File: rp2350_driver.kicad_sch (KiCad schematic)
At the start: 256 parts, among them J1 Power Input, J2 CAN2 PLUG, J201 Estop Conn, J202 USB_C_Receptacle_USB2.0, J203 Conn_01x06, J204 SM03B-SRSS-TB, J205 Power Output, J206 SM03B-SRSS-TB, J207 Conn_01x03, J208 Conn_01x03, J21 Power Input, J3 Power Input, Q1 Q_PNP_BEC, Q2 Q_PNP_BEC, Q201 Q_PNP_BEC, Q3 Q_PNP_BEC, SW201 Boot, SW202 Reset, U1 INA240A1D, U10 SIT3088ETK, U11 TS5A3159DCK, U12 SIT3088ETK, U13 TS5A3159DCK, U14 TS5A3159DCK, U15 TS5A3159DCK, U16 TS5A3159DCK, U17 TS5A3159DCK, U2 EG3113, U201 EG3113, U202 SPX3819M5-L-3-3, U203 RP2350_80QFN, U204 W25Q16JV, U21 INA240A1D, U3 USBLC6-2P6, U4 TX4137, U44 INA240A1D, U5 EG3113, U6 CA-IS3052G, U7 SIT3088ETK, U8 EG3113, U9 SIT3088ETK, Y201 ABM8-272-T3

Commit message: All components in board footprint. Big readme update.
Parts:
- added C30, C33, C34, C35, C36: 100n, Capacitor_SMD:C_0402_1005Metric, symbol Device:C
- added R21, R34, R37, R38, R39, R42, R43, R44: 10k, Resistor_SMD:R_0402_1005Metric, symbol Device:R
- added U18, U19, U20, U22: TS5A3159DCK, Package_TO_SOT_SMD:SOT-353_SC-70-5, symbol integrated:TS5A3159
- SW201, SW202: footprint Button_Switch_SMD:SW_Push_1P1T_NO_Vertical_Wuerth_434133025816 -> parts:KEY-SMD_4P-L4.2-W3.2-P2.20-LS4.6; LCSC (none) -> C19724063
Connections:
- net GPIO14 is gone; now on net V_SW: U203.13 (GPIO14)
- net GPIO15 is gone; now on net I2C_SW: U203.14 (GPIO15)
- net GPIO32 is gone; now on net HALL2: U203.40 (GPIO32)
- net GPIO33 is gone; now on net HALL3: U203.42 (GPIO33)
- net GPIO34 is gone; now on net H1_SW: U203.43 (GPIO34)
- net GPIO35 is gone; now on net H2_SW: U203.44 (GPIO35)
- net GPIO36 is gone; now on net H3_SW: U203.45 (GPIO36)
- net +3V3: now also C36.1, R21.2, R37.2, R39.2, R43.2
- net B_PHASE_SENSE: now also U22.3 (NC); no longer U203.55 (GPIO44_ADC4)
- net C_PHASE_SENSE: now also U20.3 (NC); no longer U203.56 (GPIO45_ADC5)
- net ENC_A_N: now also U14.4 (COM); no longer FL1.2
- net ENC_A_P: no longer FL1.3
- net ENC_B_N: now also U17.4 (COM); no longer FL2.2
- net ENC_B_P: now also U16.4 (COM); no longer FL2.3, U14.4 (COM)
- net ENC_C_N: now also U19.4 (COM); no longer FL3.2
- net ENC_C_P: now also U18.4 (COM); no longer FL3.3, U16.4 (COM)
- net ENC_D_N: now also R43.1, R44.2
- net ENC_D_P: now also FL4.3; no longer U17.4 (COM)
- net GND: now also C30.2, C33.2, C34.2, C35.2, C36.2, R34.1, R38.1, R42.1, R44.1, U18.2 (GND), U19.2 (GND), U20.2 (GND), U22.2 (GND)
- net HALL1: now also U203.39 (GPIO31)
- net Vdrive: now also C30.1, C33.1, C34.1, C35.1, U18.5 (V+), U19.5 (V+), U20.5 (V+), U22.5 (V+)
- net ENC_A_N_SW: now reaches U14.3 (NC)
- net ENC_A_N_SW: now also FL1.2, R39.1, R42.2
- net ENC_A_P_SW: now reaches U13.3 (NC)
- net ENC_A_P_SW: now also FL1.3
- net ENC_B_P_SW: now reaches U16.3 (NC)
- net ENC_B_P_SW: now also FL2.3
- net ENC_D_P_SWITCHED renamed ENC_B_N_SW
- net ENC_B_N_SW: now also FL2.2, R37.1, R38.2; no longer FL4.3
- net GPIO37 renamed EXT_ANALOG_SW
- net EXT_ANALOG_SW: now also U18.6 (ENB), U19.6 (ENB), U20.6 (ENB), U22.6 (ENB)
- net GPIO38: no longer names the net of U203.47 (GPIO38)
- net GPIO39: no longer names the net of U203.48 (GPIO39)
- new net ADC4: U203.55 (GPIO44_ADC4), U22.1 (NO)
- new net ADC5: U20.1 (NO), U203.56 (GPIO45_ADC5)
- new net ENC_C_N_SW: FL3.2, R21.1, R34.2, U19.3 (NC)
- new net ENC_C_P_SW: FL3.3, U18.3 (NC)
- new net EXT_ANALOG1: U18.1 (NO), U22.4 (COM)
- new net EXT_ANALOG2: U19.1 (NO), U20.4 (COM)
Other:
- note added: "Divider for single ended use without hall filtering."
- note added: "Encoder Supports: Single Ended I2C Hall Sensors Differential or Single Ended SPI Differential or Single Ended Quadrature with Index Dual Channel Analog"
- note added: "GIRL ARE YOUR ENCODERS NUMERICALLY OR ALPHABETICALLY INDEXED MAKE A GODDAMN DECISION"
- note added: "When using halls, route signals through this filter network."
- note removed: "IF ANALOG SWITCHES LET US ROUTE SINGLE ENDED TO OTHER GPIO PINS THEN WE DON'T NEED DEDICATED I2C PINS"
- note removed: "Preferred connections: Differential I2C (Will choose single ended for now) Hall Sensors (single ended) Differential SPI Differential Quadrature with Index No planned support for analog (could add SPI converter)"
- moved on the sheet: C14, C16, C19, C20, C22, C26, C27, C28, C31, C32, R19, R20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

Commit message: 100 percent routed and no DRC errors! needs massive review still.
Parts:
- C47: renamed from C219; LCSC (none) -> C15850
- U13: renamed from U20; footprint Package_TO_SOT_SMD:SOT-353_SC-70-5 -> Package_TO_SOT_SMD:SOT-363_SC-70-6
- U14: renamed from U22; footprint Package_TO_SOT_SMD:SOT-353_SC-70-5 -> Package_TO_SOT_SMD:SOT-363_SC-70-6
- U15: footprint Package_TO_SOT_SMD:SOT-353_SC-70-5 -> Package_TO_SOT_SMD:SOT-363_SC-70-6
- U17: renamed from U11; footprint Package_TO_SOT_SMD:SOT-353_SC-70-5 -> Package_TO_SOT_SMD:SOT-363_SC-70-6
- U22: renamed from U13; footprint Package_TO_SOT_SMD:SOT-353_SC-70-5 -> Package_TO_SOT_SMD:SOT-363_SC-70-6
- U23: renamed from U16; footprint Package_TO_SOT_SMD:SOT-353_SC-70-5 -> Package_TO_SOT_SMD:SOT-363_SC-70-6
- U24: renamed from U18; footprint Package_TO_SOT_SMD:SOT-353_SC-70-5 -> Package_TO_SOT_SMD:SOT-363_SC-70-6
- U25: renamed from U19; footprint Package_TO_SOT_SMD:SOT-353_SC-70-5 -> Package_TO_SOT_SMD:SOT-363_SC-70-6
- U26: renamed from U14; footprint Package_TO_SOT_SMD:SOT-353_SC-70-5 -> Package_TO_SOT_SMD:SOT-363_SC-70-6
- U27: renamed from U17; footprint Package_TO_SOT_SMD:SOT-353_SC-70-5 -> Package_TO_SOT_SMD:SOT-363_SC-70-6
- renumbered AH2 to AH1, AL2 to AL1, BH2 to BH1, BL2 to BL1, C77 to C1, C70 to C10, C10 to C11, C202 to C12, C221 to C13, C222 to C14, C11 to C15, C66 to C16, C216 to C17, C217 to C18, C4 to C19, C15 to C2, C203 to C20, C215 to C21, C204 to C22, C25 to C23, C205 to C24, C106 to C25, C105 to C26, C2 to C27, C13 to C28, C1 to C29, C12 to C3, C206 to C30, C9 to C31, C207 to C32, C103 to C33, C104 to C34, C208 to C35, C65 to C36, C209 to C37, C210 to C38, C6 to C39, C218 to C4, C74 to C40, C211 to C41, C3 to C42, C212 to C43, C78 to C44, C213 to C45, C214 to C46, C220 to C48, C34 to C49, C201 to C5, C35 to C50, C233 to C51, C29 to C52, C234 to C53, C235 to C54, C236 to C55, C36 to C56, C5 to C57, C7 to C58, C23 to C59, C17 to C6, C21 to C60, C8 to C61, C18 to C62, C24 to C63, C26 to C64, C28 to C65, C30 to C66, C19 to C67, C31 to C68, C20 to C69, C101 to C7, C32 to C70, C33 to C71, C14 to C72, C22 to C73, C16 to C74, C27 to C75, C79 to C8, C102 to C9, CH2 to CH1, CH201 to CH2, CL2 to CL1, CL201 to CL2, D202 to D1, D2 to D10, D16 to D11, D15 to D12, D8 to D13, D10 to D14, D6 to D15, D5 to D16, D9 to D17, D203 to D18, D204 to D19, D207 to D2, D205 to D20, D206 to D21, D4 to D22, D19 to D23, D20 to D24, D21 to D25, D22 to D26, D23 to D27, D7 to D3, D201 to D4, D1 to D5, D17 to D6, D14 to D7, D3 to D8, D18 to D9, FL2 to FL1, FL1 to FL2, J3 to J1, J205 to J10, J2 to J11, J203 to J12, J1 to J2, J202 to J3, J206 to J4, J201 to J5, J204 to J6, J207 to J7, J208 to J8, J21 to J9, L201 to L2, Q3 to Q1, Q1 to Q2, Q2 to Q3, Q201 to Q4, R120 to R1, R31 to R10, R30 to R11, R112 to R12, R33 to R13, R32 to R14, R36 to R15, R11 to R16, R86 to R17, R87 to R18, R12 to R19, R119 to R2, R105 to R20, R121 to R21, R122 to R22, R113 to R23, R208 to R24, R26 to R25, R211 to R26, R18 to R27, R2 to R28, R22 to R29, R238 to R3, R25 to R30, R24 to R31, R201 to R32, R23 to R33, R206 to R34, R123 to R35, R124 to R36, R91 to R37, R90 to R38, R4 to R39, R239 to R4, R5 to R40, R1 to R41, R8 to R42, R9 to R43, R7 to R44, R27 to R45, R28 to R46, R29 to R47, R88 to R48, R45 to R49, R240 to R5, R202 to R50, R203 to R51, R89 to R52, R225 to R53, R224 to R54, R109 to R55, R114 to R56, R16 to R57, R17 to R58, R6 to R59, R212 to R6, R10 to R60, R13 to R61, R204 to R62, R205 to R63, R207 to R64, R227 to R65, R228 to R66, R209 to R67, R210 to R68, R220 to R69, R213 to R7, R221 to R70, R222 to R71, R223 to R72, R229 to R73, R230 to R74, R231 to R75, R232 to R76, R233 to R77, R234 to R78, R235 to R79, R226 to R8, R236 to R80, R237 to R81, R14 to R82, R15 to R83, R35 to R84, R40 to R85, R37 to R86, R38 to R87, R39 to R88, R42 to R89, R3 to R9, R43 to R90, R44 to R91, R21 to R92, R34 to R93, R20 to R94, R41 to R95, R19 to R96, SW201 to SW1, SW202 to SW2, TP81 to TP1, TP208 to TP10, TP73 to TP2, TP74 to TP3, TP77 to TP4, TP64 to TP5, TP66 to TP6, TP94 to TP7, TP71 to TP8, TP207 to TP9, U8 to U1, U44 to U10, U3 to U11, U201 to U12, U6 to U16, U12 to U18, U7 to U19, U4 to U2, U9 to U20, U10 to U21, U204 to U3, U202 to U4, U21 to U5, U5 to U6, U2 to U7, U203 to U8, U1 to U9, Y201 to Y1
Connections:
- net +5V is gone; now on net Vdrive: C15.2, C2.2, C27.2, C48.2, D10.2 (A), D14.2 (A), D18.2 (A), D3.2 (A), U1.1 (VCC), U12.1 (VCC), U6.1 (VCC), U7.1 (VCC)
- no-connect marks 2 -> 1
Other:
- moved on the sheet: C11, C12, C3, C4, C5, D1, D2, D4, D8, J3, J4, J5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

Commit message: Cleaned up schematic encoder layout, fixed a sch/layout bug.
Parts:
- added D28, D29: 5V TVS, Package_TO_SOT_SMD:SOT-883, symbol Power_Protection:SP0502BAHT
- added TP12, TP13, TP14, TP15, TP16, TP17, TP18, TP19: TestPoint, TestPoint:TestPoint_Pad_D1.0mm, symbol Connector:TestPoint
- C11, C47: value 10u -> 10u 25v
- C12, C5: value 10u -> 10u 25v; LCSC (none) -> C15850
- C15, C2, C27, C48, C58: LCSC C162274 -> C329940
- C20, C24, C30, C32, C35, C37, C38, C41, C43, C45, C46: LCSC C14663 -> C131394
- C67, C68, C74: LCSC C60137 -> C20069324
- D13, D17, D21, D9: LCSC C726760 -> C366557
- J1, J2: value Power Input -> XT30; LCSC C2918078 -> C431092; Note (none) -> Phase Output
- J10: LCSC C7363338 -> C2913282
- J4, J6: LCSC C160403 -> C2763613
- J7: LCSC (none) -> C492411
- J8: LCSC (none) -> C2897385
- J9: value Power Input -> XT30; LCSC C2918078 -> C431092; Name (none) -> Power Input
- L2: LCSC (none) -> C42411119
- R3, R4, R59, R60, R62, R63, R67, R68, R70, R71: LCSC C304067 -> C861451
- R32: value 33 -> 33R; LCSC (none) -> C25105
- R53, R54: value 100 -> 100R
- SW1: value Boot -> Button; Name (none) -> Boot
- SW2: value Reset -> Button; Name (none) -> Reset
- U16: value CA-IS3052G -> CA-IS3052CG; LCSC C528764 -> C41784142
- U8: LCSC (none) -> C42415655
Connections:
- net ADC4: now also U14.4 (COM); no longer U14.1 (NO)
- net ADC5: now also U13.4 (COM); no longer U13.1 (NO)
- net A_PWM_H: now also TP14.1
- net A_PWM_L\: now also TP15.1
- net B_PWM_H: now also TP17.1
- net B_PWM_L\: now also TP16.1
- net C_PWM_H: now also TP12.1
- net C_PWM_L\: now also TP13.1
- net D_PWM_H: now also TP19.1
- net D_PWM_L\: now also TP18.1
- net EXT_ANALOG1: now also U14.1 (NO); no longer U14.4 (COM)
- net EXT_ANALOG2: now also U13.1 (NO); no longer U13.4 (COM)
- net GND: now also D28.3 (A), D29.3 (A)
- net RXI_INTERBOARD_1: now also D28.2 (K)
- net RXI_INTERBOARD_2: now also D29.2 (K)
- net TXO_INTERBOARD_1: now also D28.1 (K)
- net TXO_INTERBOARD_2: now also D29.1 (K)
- net ENC1_D renamed ENC_A_DATA
- net ENC1_E renamed ENC_A_SW
- net ENC2_D renamed ENC_B_DATA
- net ENC2_E renamed ENC_B_SW
- net ENC3_D renamed ENC_C_DATA
- net ENC3_E renamed ENC_C_SW
- net ENC4_D renamed ENC_D_DATA
- net ENC4_E renamed ENC_D_SW
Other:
- note added: "CPU: Analog Halls I2C"
- note added: "CPU: Single Ended I/O"
- note added: "Differential tranceivers"
- note added: "EXT_ANALOG_SW can be shared. We either read external lines or those go to differential transceivers and we read B and C phase sense with analog."
- note added: "Encoder I/O"
- note added: "I/O Switching"
- note added: "Motor Phase B/C Sense"
- note removed: "GIRL ARE YOUR ENCODERS NUMERICALLY OR ALPHABETICALLY INDEXED MAKE A GODDAMN DECISION"
- moved on the sheet: C47, C49, C50, C59, C60, C61, C62, C63, C64, C65, C66, C67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

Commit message: Added USB-C PD, updated silk.
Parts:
- removed D4: B5819W SL, Diode_SMD:D_SOD-123, symbol Diode:MBR340
- removed R5: 5.1k 0.1%, Resistor_SMD:R_0603_1608Metric, symbol MotorController:TAYLOR_RESISTOR
- added C105, C106, C78: 4.7uF 50V X5R, Capacitor_SMD:C_0805_2012Metric, symbol Device:C
- added C107, C108: 330pF 50V, Capacitor_SMD:C_0402_1005Metric, symbol Device:C
- added C76: 100n, Capacitor_SMD:C_0402_1005Metric, symbol Device:C
- added C77: 4.7u, Capacitor_SMD:C_0402_1005Metric, symbol Device:C
- added R5: 470k, Resistor_SMD:R_0402_1005Metric, symbol Device:R
- added TP20: TestPoint, TestPoint:TestPoint_Pad_D1.0mm, symbol Connector:TestPoint
- added U101: FUSB302BMPX, Package_DFN_QFN:WQFN-14-1EP_2.5x2.5mm_P0.5mm_EP1.45x1.45mm, symbol Interface_USB:FUSB302BMPX
- added U28: LM73100RPWR, LM73100RPWR:IC_LM73100RPWR, symbol LM73100RPWR:LM73100RPWR
- R6: value 5.1k -> 165k; footprint Resistor_SMD:R_0603_1608Metric -> Resistor_SMD:R_0402_1005Metric; LCSC C23186 -> (none)
- R7: value 5.1k -> 39.2k; footprint Resistor_SMD:R_0603_1608Metric -> Resistor_SMD:R_0402_1005Metric; LCSC C23186 -> (none)
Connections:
- net +3V3: now also C76.1, C77.1, U101.12 (VCONN), U101.13 (VCONN), U101.3 (VDD), U101.4 (VDD)
- net A_N: now also D17.1 (A1), J1.1 (Pin_1), R55.2, R56.2, U10.8 (+); no longer D9.1 (A1), J2.1 (Pin_1), R20.2, R23.2, U5.8 (+)
- net C_N: now also D9.1 (A1), J2.1 (Pin_1), R20.2, R23.2, U5.8 (+); no longer D17.1 (A1), J1.1 (Pin_1), R55.2, R56.2, U10.8 (+)
- net GND: now also R7.1, C105.2, C106.2, C107.1, C108.1, C76.2, C77.2, C78.2, U101.15 (GND), U101.8 (GND), U101.9 (GND), U28.8 (GND), U28.9 (IMON); no longer R6.1, R7.2
- net I2C_SCL: now also U101.6 (SCL)
- net I2C_SDA: now also U101.7 (SDA)
- net VBUS: now also C105.1, C106.1, R5.2, U101.2 (VBUS), U28.5 (IN)
- net VMOT: now also C78.1, U28.6 (OUT)
- net at J3.B5 (CC2): now also C107.2, U101.1 (CC2), U101.14 (CC2); no longer R7.1
- net at U8.47 (GPIO38): now also TP20.1
- net PD_INT: now reaches U8.48 (GPIO39)
- net PD_INT: now also U101.5 (INT_N)
- net at R6.2: now also R5.1, U28.1 (EN/UVLO); no longer J3.A5 (CC1)
- new net: R6.1, R7.2, U28.2 (OVLO)
- new net: C108.2, J3.A5 (CC1), U101.10 (CC1), U101.11 (CC1)
- no-connect marks 1 -> 4
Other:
- note added: "Additional Switching"
- note added: "EXT_ANALOG_SW can be shared. We either route external lines to the ADC or those lines go to differential transceivers and we read B and C phase sense with analog."
- note added: "R1 = R2/((Vout/0.812V)-1) Resistor vals for 5v out given in datasheet."
- note removed: "EXT_ANALOG_SW can be shared. We either read external lines or those go to differential transceivers and we read B and C phase sense with analog."
- moved on the sheet: D2, D28, D29, J3

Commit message: Update schematic size, add PDF schematic.
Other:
- moved on the sheet: AL1, BH1, BL1, C1, C10, C105, C106, C107, C108, C11, C12, C13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

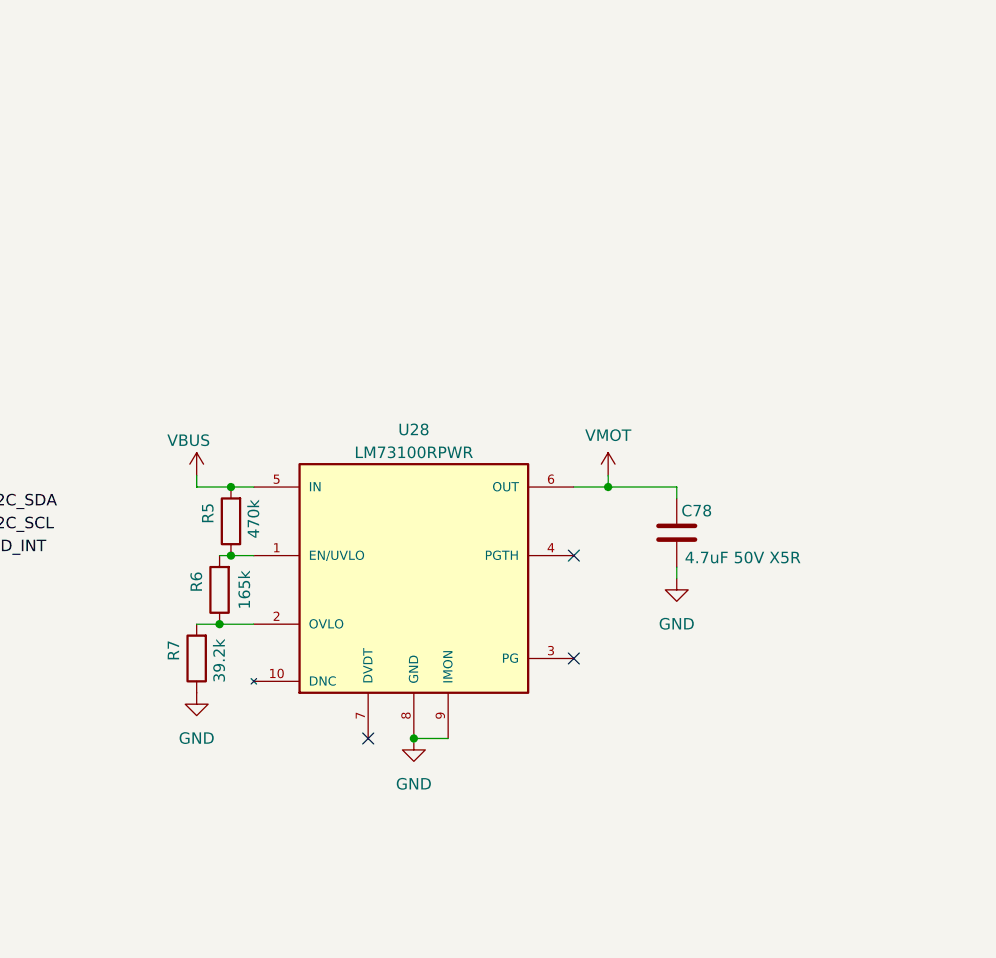
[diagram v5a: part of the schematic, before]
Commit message: Swap ideal diode to something which supports VMOT
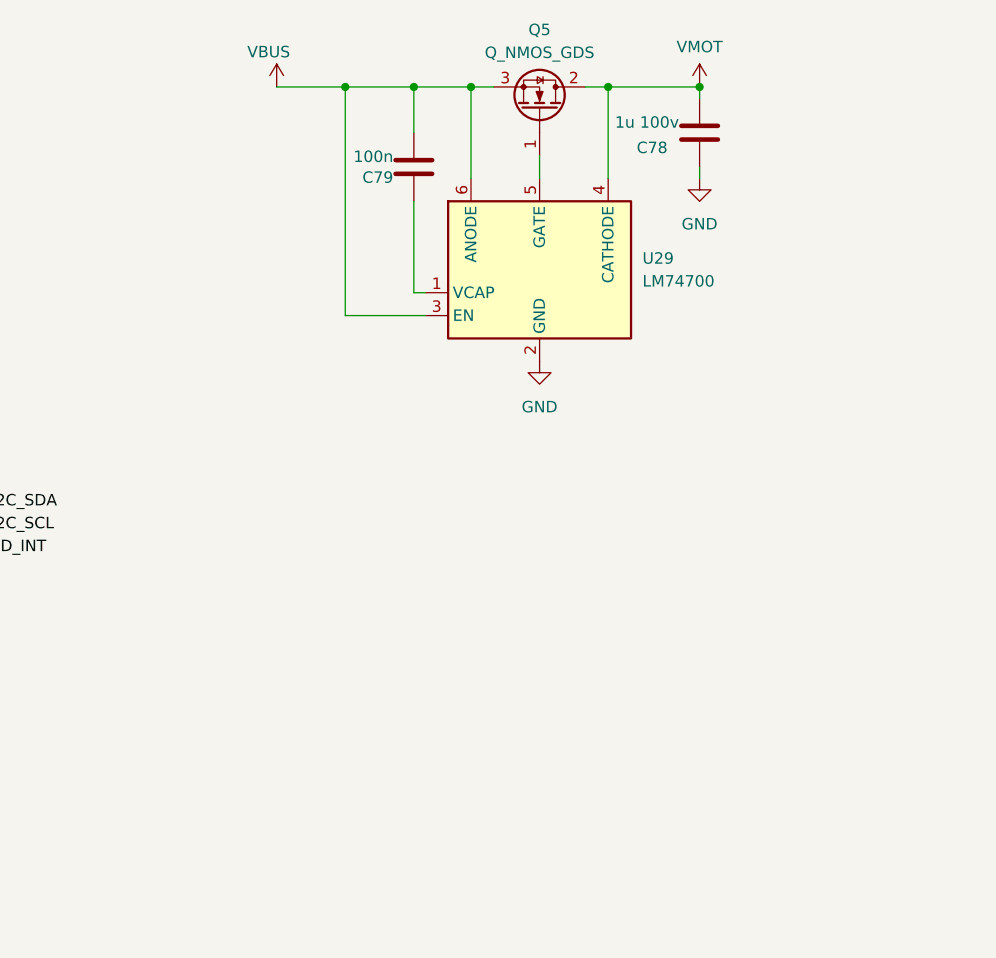
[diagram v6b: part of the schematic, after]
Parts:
- removed R5: 470k, Resistor_SMD:R_0402_1005Metric, symbol Device:R
- removed R6: 165k, Resistor_SMD:R_0402_1005Metric, symbol Device:R
- removed R7: 39.2k, Resistor_SMD:R_0402_1005Metric, symbol Device:R
- removed U28: LM73100RPWR, LM73100RPWR:IC_LM73100RPWR, symbol LM73100RPWR:LM73100RPWR
- added C79: 100n, Capacitor_SMD:C_0402_1005Metric, symbol Device:C
- added Q5: Q_NMOS_GDS, Package_TO_SOT_SMD:SOT-89-3, symbol Transistor_FET:Q_NMOS_GDS
- added U29: LM74700, Package_TO_SOT_SMD:SOT-23-6, symbol Power_Management:LM74700
- C78: value 4.7uF 50V X5R -> 1u 100v; footprint Capacitor_SMD:C_0805_2012Metric -> Capacitor_SMD:C_0603_1608Metric; LCSC C98192 -> C23829972
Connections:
- net GND: now also C78.1, U29.2 (GND); no longer C78.2
- net VBUS: now also C79.2, Q5.3 (S), U29.3 (EN), U29.6 (ANODE)
- net VMOT: now also C78.2, Q5.2 (D), U29.4 (CATHODE); no longer C78.1
- new net: C79.1, U29.1 (VCAP)
- new net: Q5.1 (G), U29.5 (GATE)
- no-connect marks 4 -> 1

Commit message: bunch of small trace cleanup
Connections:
- net CAN0_N: now also D22.1 (K); no longer D22.2 (K)
- net CAN0_P: now also D22.2 (K); no longer D22.1 (K)
- net ENC_C_N: now also D25.1 (K); no longer D25.2 (K)
- net ENC_C_P: now also D25.2 (K); no longer D25.1 (K)
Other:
- moved on the sheet: C11, C12, C3, C47, C5, C78, C79, D2, D28, D29, D8, J7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

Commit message: Silly but complete routing of the 80v power supply
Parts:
- removed C11: 10u 25v, Capacitor_SMD:C_0805_2012Metric, symbol Device:C
- removed D2: 3.3v Zener, Diode_SMD:D_SOD-123, symbol Device:D_Zener
- removed D8: SS310, Diode_SMD:D_SOD-123F, symbol Diode:MBR340
- removed L1: 22uH 680mA, parts:IND-SMD_L3.0-W3.0_FNR30XXS, symbol Device:L
- removed R16: 23.7k, Resistor_SMD:R_0402_1005Metric, symbol Device:R
- removed R19: 124k, Resistor_SMD:R_0402_1005Metric, symbol Device:R
- removed R3, R4: 50k 0.1%, Resistor_SMD:R_0603_1608Metric, symbol MotorController:TAYLOR_RESISTOR
- removed U2: TX4137, Package_TO_SOT_SMD:SOT-23-6, symbol integrated:TX4137
- added C11: 100uF ±20% 10V, Capacitor_SMD:CP_Elec_5x5.4, symbol Device:C_Polarized
- added C80: 220uF 63V solid, Capacitor_THT:CP_Radial_D10.0mm_P5.00mm, symbol Device:C_Polarized
- added C81: 1uf 100v, Capacitor_SMD:C_0603_1608Metric, symbol Device:C
- added D4: SS210, Diode_SMD:D_SMA, symbol Diode:MBR340
- added JP1: Jumper_2_Open, Jumper:SolderJumper-2_P1.3mm_Bridged_RoundedPad1.0x1.5mm, symbol Jumper:Jumper_2_Open
- added L3: 47uH 1A, Inductor_SMD:L_APV_ANR5045, symbol Device:L
- added R5: 10k, Resistor_SMD:R_0402_1005Metric, symbol Device:R
- added R6: 3.3k, Resistor_SMD:R_0402_1005Metric, symbol Device:R
- added U28: XL7005A, Package_SO:SOIC-8-1EP_3.9x4.9mm_P1.27mm_EP2.29x3mm, symbol integrated:XL7005A
- C3: value 4.7uF 100v -> 33n; footprint Capacitor_SMD:C_1210_3225Metric -> Capacitor_SMD:C_0402_1005Metric; LCSC C381466 -> C106862
- C39: value 220uF 63V solid -> 100uF 100V; LCSC C5455531 -> C2887236; MPN 2210631013R00 -> 1011001013R00
- D10, D14, D18, D3: value FR107 -> DSS110; footprint Diode_SMD:D_SOD-123 -> Diode_SMD:D_SOD-123F; LCSC C511885 -> C2923942
- D5: value SMDJ51CA -> SMDJ85A; LCSC C406702 -> C2990214
- R25, R41, R73, R9: value 0R -> 4.7R; LCSC C21189 -> C2907035
- U29: LCSC (none) -> C2941042
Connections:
- net GND: now also C11.2, C80.2, C81.2, D4.2 (A), R6.1, U28.4 (EN), U28.5 (GND), U28.6 (GND), U28.7 (GND), U28.8 (GND), U28.9 (GND); no longer C3.2
- net VMOT: now also C80.1, C81.1, JP1.2 (B), U28.1 (VIN); no longer C3.1, C78.2, Q5.2 (D), U29.4 (CATHODE)
- net Vdrive: now also C3.1, C11.1, L3.2, R5.2
- new net: C78.2, JP1.1 (A), Q5.2 (D), U29.4 (CATHODE)
- new net: C3.2, R5.1, R6.2, U28.3 (FB)
- new net: D4.1 (K), L3.1, U28.2 (SW)
- no-connect marks 1 -> 0
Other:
- note added: "80 volt components, derate to 65-70 volts for operation 20 Amp max continuous current draw (estimated, depends on thermals) 50 Amp peak absolute maximum"
- note added: "Sits directly under motor capacitors so no separate large input capacitance."
- note removed: "53V input maximum run voltage 20 Amp max continuous current draw (roughly, depends on thermals) 50 Amp peak per motor absolute maximum"
- note removed: "R1 = R2/((Vout/0.812V)-1) Resistor vals for 5v out given in datasheet."
- moved on the sheet: C105, C106, C107, C108, C12, C5, C76, C77, C78, C79, J3, J6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
